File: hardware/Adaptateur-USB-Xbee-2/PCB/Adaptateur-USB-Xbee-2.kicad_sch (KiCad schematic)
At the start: 30 parts, among them J1 Conn_Coaxial, J2 USB_C_Receptacle_USB2.0, SW1 SW_Push, SW2 SW_SPDT, U1 FT231XS, U2 NCP1117-3.3_SOT223, U3A1 XBee_RR_MMT, U3B1 XBEE-3-TH, U4 74AHC1G08

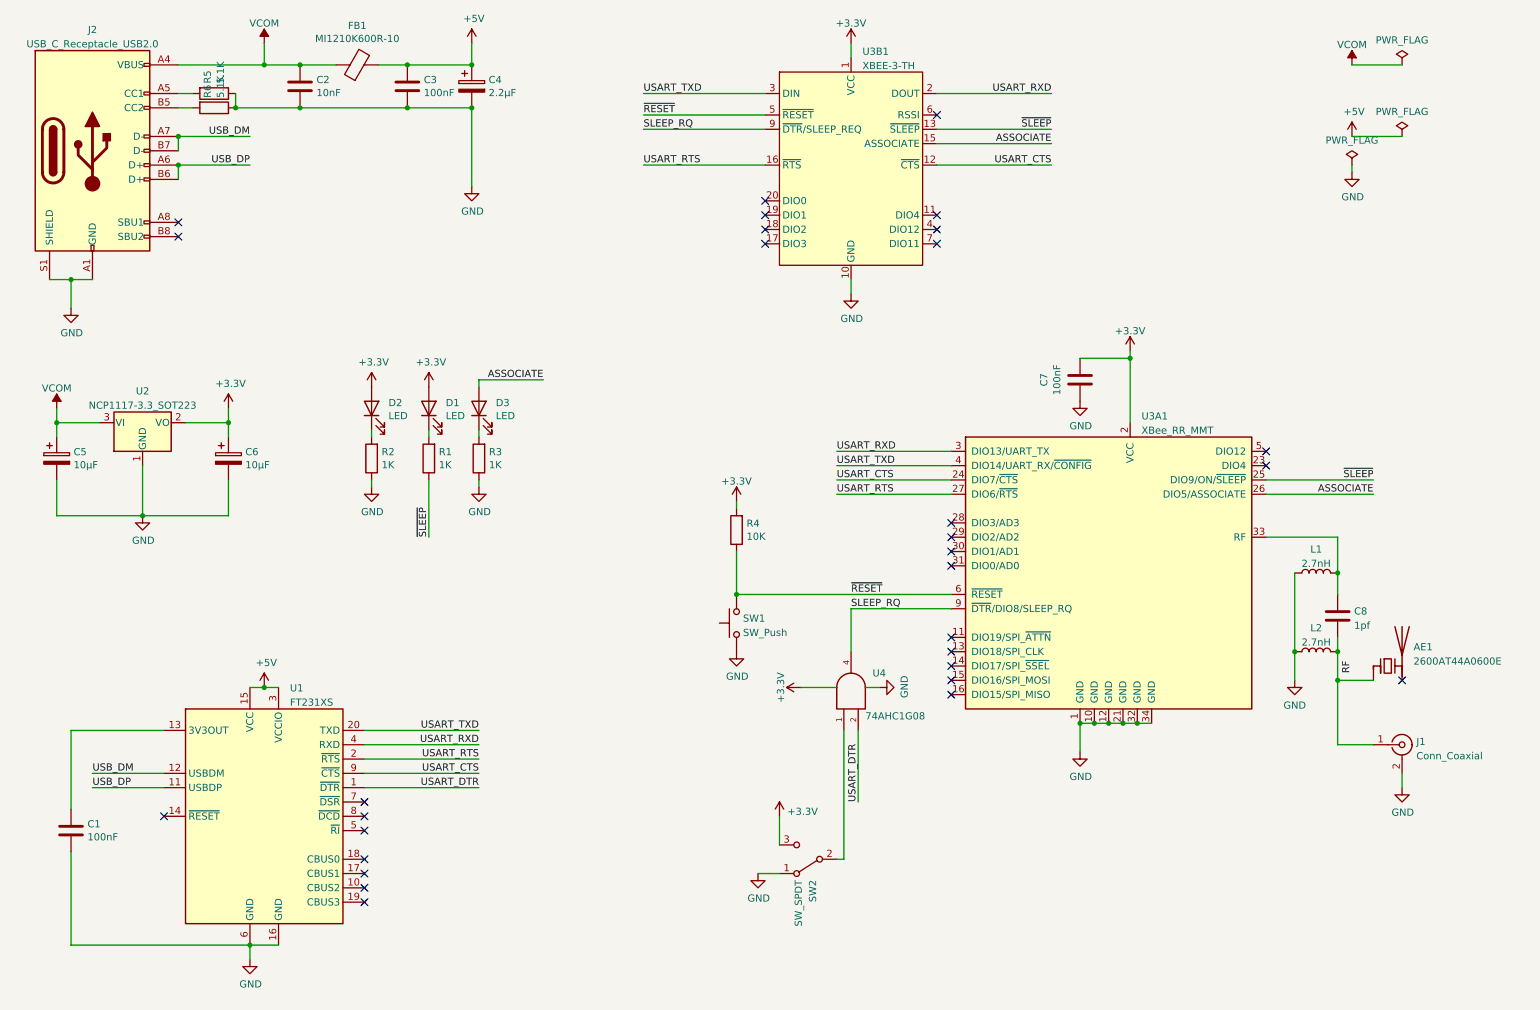
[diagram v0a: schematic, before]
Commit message: Corrections mineurs sur le PCB, V1.1
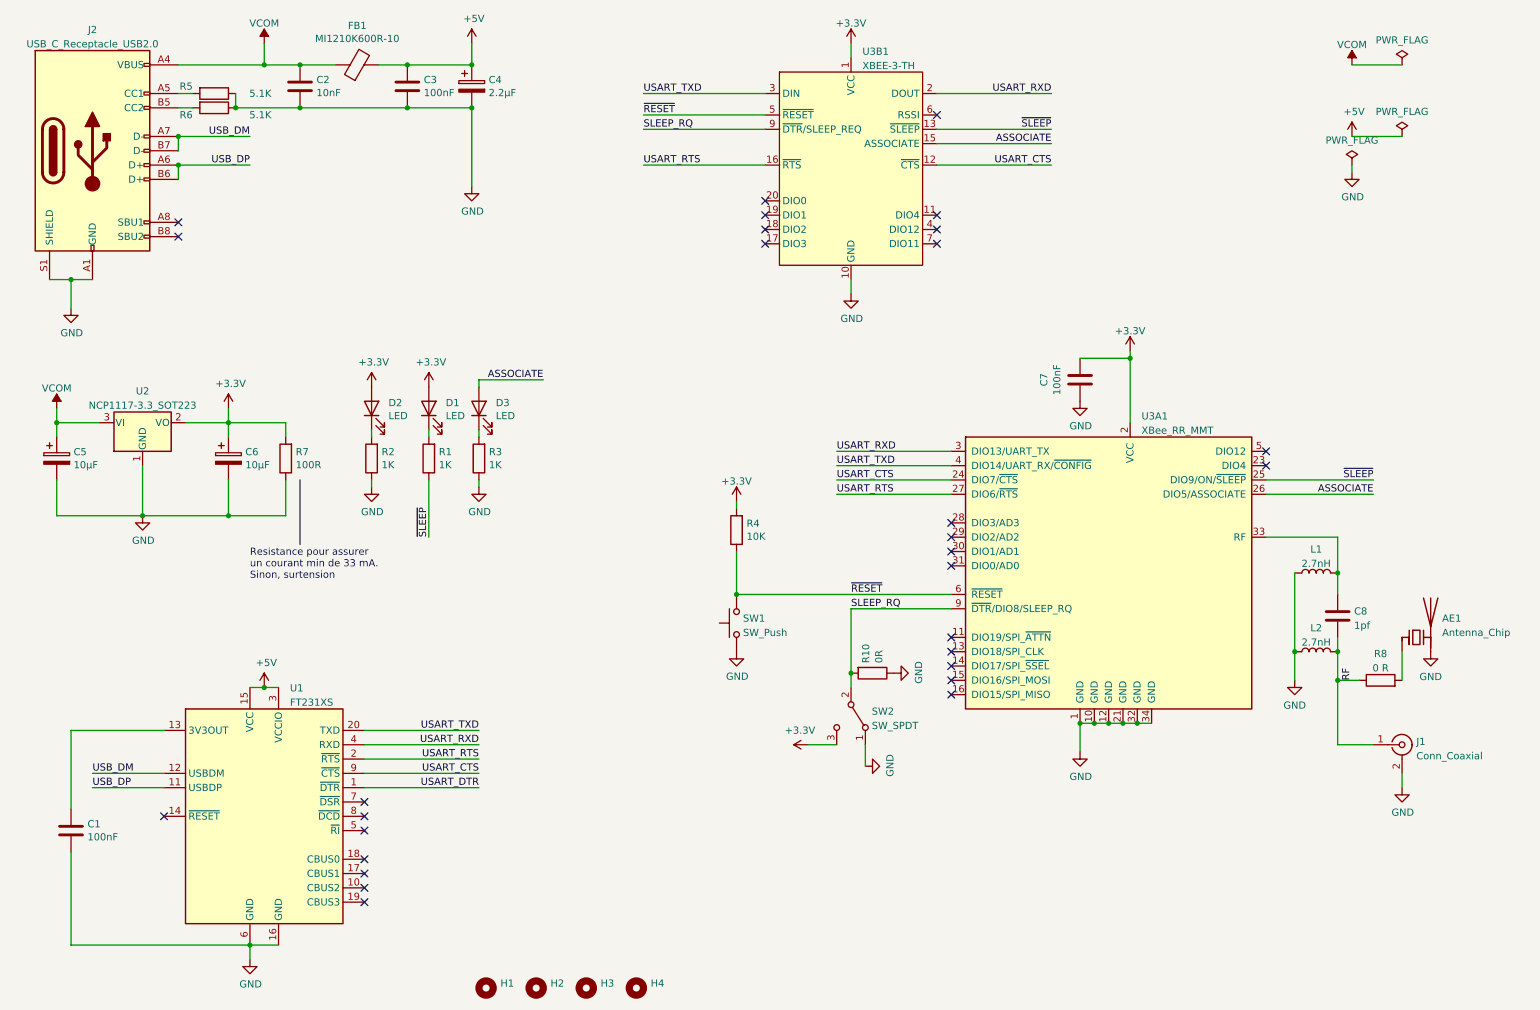
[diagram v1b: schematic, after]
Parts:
- removed U4: 74AHC1G08, Package_TO_SOT_SMD:SOT-23-5, symbol 74xGxx:74AHC1G08
- added H1, H2, H3, H4: MountingHole, MountingHole:MountingHole_3.2mm_M3, symbol Mechanical:MountingHole
- added R10: 0R, Resistor_SMD:R_1206_3216Metric, symbol Device:R
- added R7: 100R, Resistor_SMD:R_1206_3216Metric, symbol Device:R
- added R8: 0 R, Resistor_SMD:R_0805_2012Metric, symbol Device:R
- AE1: value 2600AT44A0600E -> Antenna_Chip; footprint INSA:Johanson_2600AT44A0600E -> RF_Antenna:Texas_SWRA117D_2.4GHz_Left
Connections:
- net +3.3V: now also R7.2
- net GND: now also AE1.2 (PCB_Trace), R10.1, R7.1
- net RF: now also C8.2, J1.1 (In), L2.2, R8.1
- net SLEEP_RQ: now also SW2.2 (B), R10.2
- new net: AE1.1 (FEED), R8.2
- no-connect marks 30 -> 29
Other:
- note added: "Resistance pour assurer un courant min de 33 mA. Sinon, surtension"
- company: INSA - DGEI -> INSA - GEI
- moved on the sheet: SW2

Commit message: Commit avant nouveau projet
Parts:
- removed C5, C6: 10µF, Capacitor_Tantalum_SMD:CP_EIA-6032-28_Kemet-C_Pad2.25x2.35mm_HandSolder, symbol Device:C_Polarized
- added C5: 10µF, Capacitor_SMD:C_1206_3216Metric, symbol Device:C
- added C6: 22µF, Capacitor_SMD:C_1206_3216Metric, symbol Device:C
- U2: value NCP1117-3.3_SOT223 -> AZ1117IH-3.3_SOT223
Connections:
- net +3.3V: now also C6.1
- net GND: now also C5.2, C6.2
- net VCOM: now also C5.1
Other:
- note added: "Note pour la prochaine revision: Retirer VCCIO du 5V et le mettre sur le 3V de la puce FTDI Ça doit etre la cause des surtensions sur le regulateur les IO sont en 5V et les alim en 3v3"
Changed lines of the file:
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@@
+    (stroke (width 0) (type default) (color 0 0 0 0))
+  )
+  (polyline (pts (xy 68.58 134.62) (xy 86.36 134.62))
     (stroke (width 0) (type default) (color 0 0 0 0))
   )
@@
     (effects (font (size 1.27 1.27)) (justify left bottom))
   )
+  (text "Note pour la prochaine revision:\nRetirer VCCIO du 5V et le mettre sur le 3V\nde la puce FTDI\nÇa doit etre la cause des surtensions sur le regulateur\nles IO sont en 5V et les alim en 3v3"
+    (at 72.39 133.35 0)
+    (effects (font (size 1.27 1.27)) (justify left bottom))
+  )
   (label "USART_RTS" (at 163.83 102.87 0)
     (effects (font (size 1.27 1.27)) (justify left bottom))
@@
     )
     (pin "1")
+  )
+  (symbol (lib_id "Device:C") (at 55.88 96.52 0) (unit 1)
+    (in_bom yes) (on_board yes)
+    (property "Reference" "C6" (id 0) (at 58.801 95.3516 0)
+      (effects (font (size 1.27 1.27)) (justify left))
+    )
+    (property "Value" "22µF" (id 1) (at 58.801 97.663 0)
+      (effects (font (size 1.27 1.27)) (justify left))
+    )
+    (property "Footprint" "Capacitor_SMD:C_1206_3216Metric" (id 2) (at 56.8452 100.33 0)
+      (effects (font (size 1.27 1.27)) hide)
+    )
+    (property "Datasheet" "~" (id 3) (at 55.88 96.52 0)
+      (effects (font (size 1.27 1.27)) hide)
+    )
+    (pin "1")
+    (pin "2")
   )
   (symbol (lib_id "power:PWR_FLAG") (at 264.16 26.67 0) (unit 1)
@@
     (pin "2")
   )
-  (symbol (lib_id "Device:C_Polarized") (at 25.4 96.52 0) (unit 1)
-    (in_bom yes) (on_board yes)
-    (property "Reference" "C5" (id 0) (at 28.3972 95.3516 0)
-      (effects (font (size 1.27 1.27)) (justify left))
-    )
-    (property "Value" "10µF" (id 1) (at 28.3972 97.663 0)
-      (effects (font (size 1.27 1.27)) (justify left))
-    )
-    (property "Footprint" "Capacitor_Tantalum_SMD:CP_EIA-6032-28_Kemet-C_Pad2.25x2.35mm_HandSolder" (id 2) (at 26.3652 100.33 0)
-      (effects (font (size 1.27 1.27)) hide)
-    )
-    (property "Datasheet" "~" (id 3) (at 25.4 96.52 0)
-      (effects (font (size 1.27 1.27)) hide)
-    )
-    (pin "1")
-    (pin "2")
-  )
   (symbol (lib_id "Device:FerriteBead") (at 78.74 26.67 90) (unit 1)
     (in_bom yes) (on_board yes)
@@
     )
     (pin "1")
-  )
-  (symbol (lib_id "Device:C_Polarized") (at 55.88 96.52 0) (unit 1)
-    (in_bom yes) (on_board yes)
-    (property "Reference" "C6" (id 0) (at 58.8772 95.3516 0)
-      (effects (font (size 1.27 1.27)) (justify left))
-    )
-    (property "Value" "10µF" (id 1) (at 58.8772 97.663 0)
-      (effects (font (size 1.27 1.27)) (justify left))
-    )
-    (property "Footprint" "Capacitor_Tantalum_SMD:CP_EIA-6032-28_Kemet-C_Pad2.25x2.35mm_HandSolder" (id 2) (at 56.8452 100.33 0)
-      (effects (font (size 1.27 1.27)) hide)
-    )
-    (property "Datasheet" "~" (id 3) (at 55.88 96.52 0)
-      (effects (font (size 1.27 1.27)) hide)
-    )
-    (pin "1")
-    (pin "2")
   )
   (symbol (lib_id "Insa:XBEE-3-TH") (at 166.37 64.77 0) (unit 1)
@@
     (in_bom yes) (on_board yes) (fields_autoplaced)
     (property "Reference" "U2" (id 0) (at 40.64 84.5652 0))
-    (property "Value" "NCP1117-3.3_SOT223" (id 1) (at 40.64 87.1021 0))
+    (property "Value" "AZ1117IH-3.3_SOT223" (id 1) (at 40.64 87.1021 0))
     (property "Footprint" "Package_TO_SOT_SMD:SOT-223-3_TabPin2" (id 2) (at 40.64 85.09 0)
       (effects (font (size 1.27 1.27)) hide)
@@
     (pin "2")
   )
+  (symbol (lib_id "Device:C") (at 25.4 96.52 0) (unit 1)
+    (in_bom yes) (on_board yes)
+    (property "Reference" "C5" (id 0) (at 28.321 95.3516 0)
+      (effects (font (size 1.27 1.27)) (justify left))
+    )
+    (property "Value" "10µF" (id 1) (at 28.321 97.663 0)
+      (effects (font (size 1.27 1.27)) (justify left))
+    )
+    (property "Footprint" "Capacitor_SMD:C_1206_3216Metric" (id 2) (at 26.3652 100.33 0)
+      (effects (font (size 1.27 1.27)) hide)
+    )
+    (property "Datasheet" "~" (id 3) (at 25.4 96.52 0)
+      (effects (font (size 1.27 1.27)) hide)
+    )
+    (pin "1")
+    (pin "2")
+  )
   (symbol (lib_id "power:+5V") (at 99.06 22.86 0) (unit 1)
     (in_bom yes) (on_board yes)
@@
       (reference "C4") (unit 1) (value "2.2µF") (footprint "Capacitor_Tantalum_SMD:CP_EIA-3528-21_Kemet-B_Pad1.50x2.35mm_HandSolder")
     )
-    (path "/63b3a643-fee7-4d6f-8436-d6d8bb8a8990"
-      (reference "C5") (unit 1) (value "10µF") (footprint "Capacitor_Tantalum_SMD:CP_EIA-6032-28_Kemet-C_Pad2.25x2.35mm_HandSolder")
-    )
-    (path "/880b3454-936b-4144-a78f-2439a9b80d58"
-      (reference "C6") (unit 1) (value "10µF") (footprint "Capacitor_Tantalum_SMD:CP_EIA-6032-28_Kemet-C_Pad2.25x2.35mm_HandSolder")
+    (path "/f496638e-f7a1-4b1e-a3b6-693c949eeed3"
+      (reference "C5") (unit 1) (value "10µF") (footprint "Capacitor_SMD:C_1206_3216Metric")
+    )
+    (path "/183f0144-18f2-4586-88bf-b3e761d702ee"
+      (reference "C6") (unit 1) (value "22µF") (footprint "Capacitor_SMD:C_1206_3216Metric")
     )
     (path "/4143c9b4-b3e8-4a83-bc78-cc7aff0d8d87"
@@
     )
     (path "/9c7e4a69-e4a6-4ab2-9e11-15edc946cbde"
-      (reference "U2") (unit 1) (value "NCP1117-3.3_SOT223") (footprint "Package_TO_SOT_SMD:SOT-223-3_TabPin2")
+      (reference "U2") (unit 1) (value "AZ1117IH-3.3_SOT223") (footprint "Package_TO_SOT_SMD:SOT-223-3_TabPin2")
     )
     (path "/560abb9b-3723-49fc-8edd-c453f7f7c443"
